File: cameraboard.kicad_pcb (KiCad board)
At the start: 4 copper layers, 46.1 x 45.6 mm, 93 parts, among them J1 USB_C_Receptacle_USB2.0, J2 02x05 M 1.27mm, J3 USD-1040310811, J4 MOLEX_5051102491, J5 TFM-110-12-X-D-A, J6 FLE-107-01-X-DV-A, Q1 SQ3495EV-T1, SW1 CAS-120TA, SW2 KMR2x, SW3 CAS-120TA, U1 STM32H743VITx, U2 WE-TVS-82400102, U3 XC6210B332MR-G, U4 AP7366-28W5-7, U5 TLV75515PDBVR, U6 LTC4412xS6, Y1 12MHz/7pF

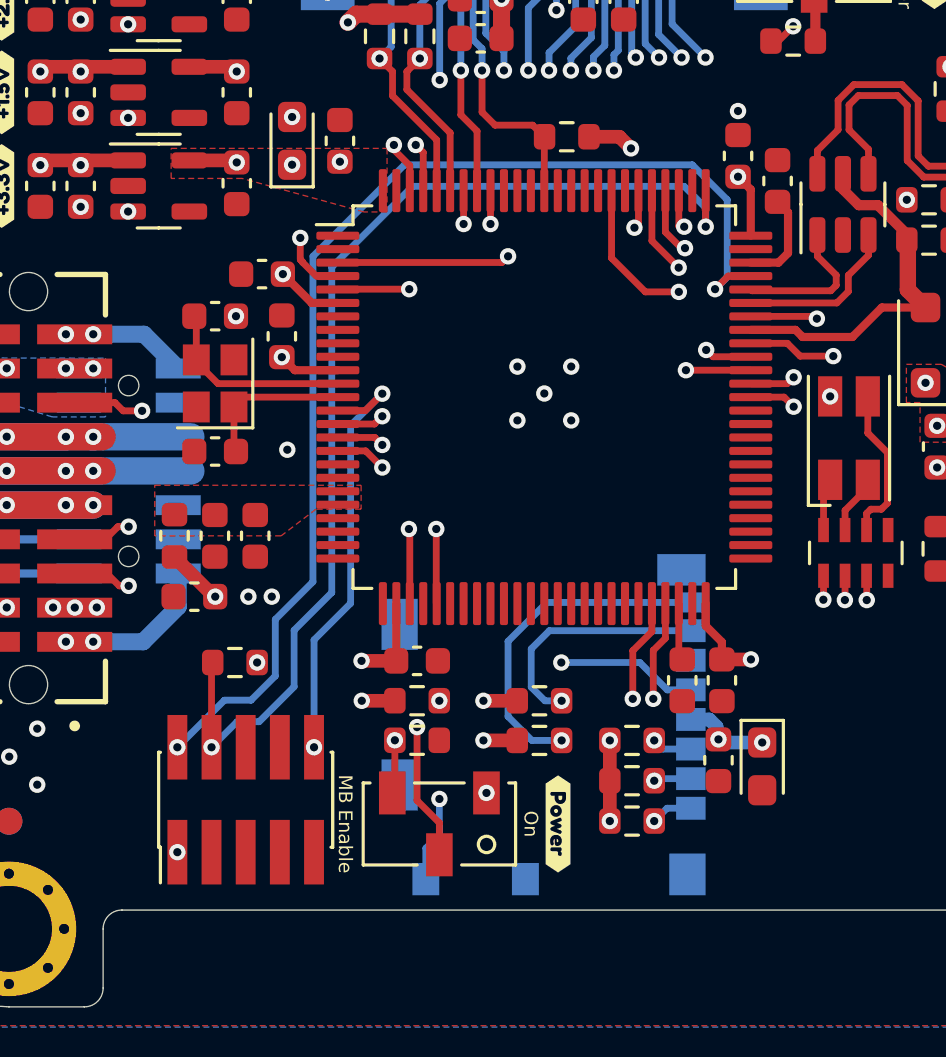
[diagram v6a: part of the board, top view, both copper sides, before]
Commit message: Moved SD card connector to allow removal with rails installed
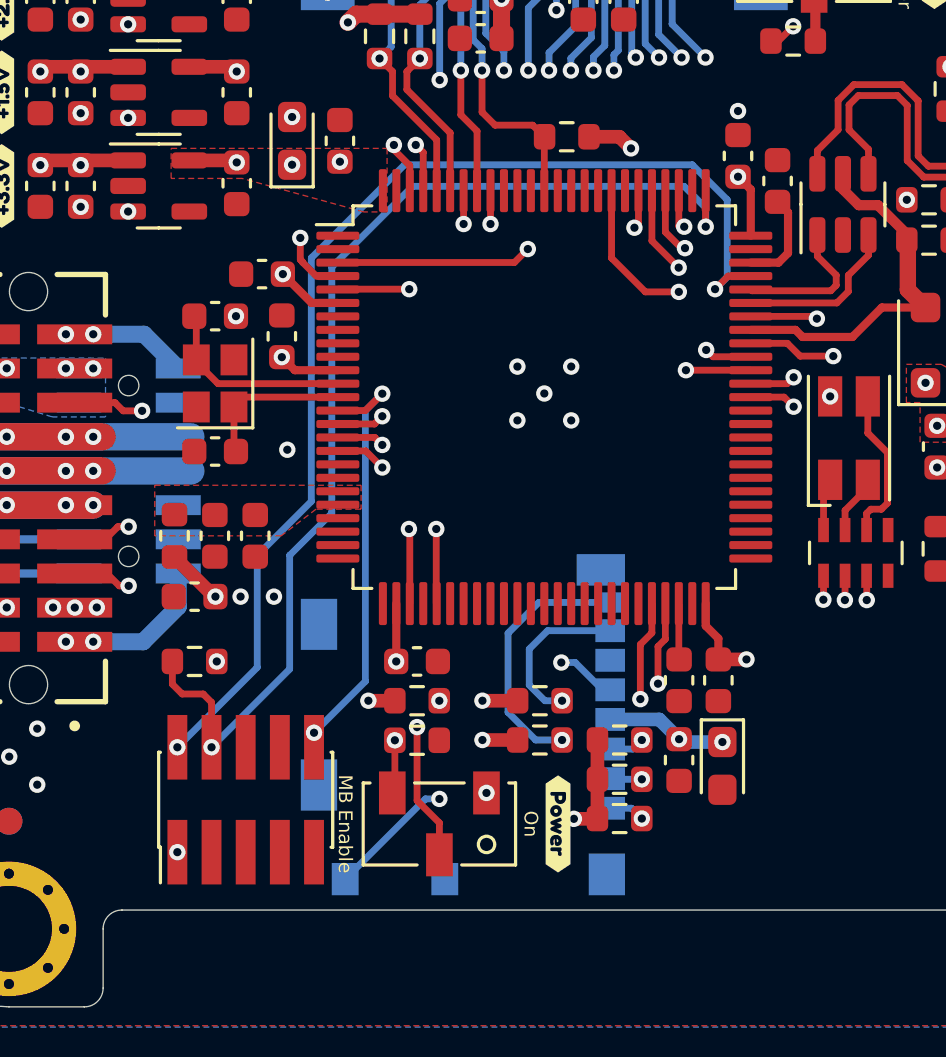
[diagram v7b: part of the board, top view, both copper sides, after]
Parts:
- moved J3 3.00 mm to (100.0, 78.5)
- moved Ref** 1.90 mm to (116.2, 78.2)
- moved R8 1.50 mm to (90.0, 76.2)
- moved C19 1.48 mm to (109.6, 80.0)
- moved C20 1.46 mm to (108.0, 79.8)
- moved R13 0.47 mm to (105.8, 82.0)
- moved R14 0.46 mm to (105.8, 80.5)
- moved R10 0.46 mm to (105.8, 79.1)
- moved C3 0.13 mm to (109.5, 76.9)
- moved C4 0.12 mm to (108.0, 76.9)
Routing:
- net /SDIO_CLK: track 25.5 -> 22.5 mm
- net /SDIO_D1: track 31.1 -> 28.2 mm
- net /SDIO_D0: track 25.6 -> 22.7 mm
- net /SD_CD: track 28.9 -> 30.4 mm
- net /SDIO_D2: track 32.9 -> 32.1 mm
- net /SDIO_D3: track 31.0 -> 30.4 mm
- net /SDIO_CMD: track 30.9 -> 30.2 mm
- net /SWCLK: track 40.9 -> 41.5 mm
- net /SWDIO: track 43.3 -> 42.7 mm
- net /NRST: track 48.5 -> 48.0 mm
- net +3.3V: track 32.3 -> 32.8 mm, vias 23 -> 22
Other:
- board text added: "18-JUN-23"
- board text removed: "12-JUN-23"

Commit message: PCB cleanup
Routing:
- net /UART3_RX: track 29.2 -> 28.0 mm
- net /UART3_TX: track 27.6 -> 26.5 mm
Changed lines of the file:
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@@
     (pts (xy 80.2 46.3) (xy 125.8 46.3))
     (height -6.93)
-    (gr_text "1795.2756 mils" (at 103 38.22) (layer "Dwgs.User")
+    (gr_text "45.6000 mm" (at 103 38.22) (layer "Dwgs.User")
       (effects (font (size 1 1) (thickness 0.15)))
     )
@@
     (pts (xy 83.1 43.4) (xy 83.100001 89))
     (height 7.157423)
-    (gr_text "1795.2756 mils" (at 77.092578 66.2 270.0000025) (layer "Dwgs.User")
+    (gr_text "45.6000 mm" (at 77.092578 66.2 270.0000025) (layer "Dwgs.User")
       (effects (font (size 1 1) (thickness 0.15)))
     )
@@
   )
   (segment (start 108 74.0094) (end 108 76.075) (width 0.254) (layer "F.Cu") (net 1))
-  (segment (start 108 76.075) (end 108.01 76.085) (width 0.254) (layer "F.Cu") (net 1))
   (segment (start 90.7273 73.7512) (end 89.2542 72.2781) (width 0.508) (layer "F.Cu") (net 2))
   (segment (start 100.7 77.62) (end 102 77.62) (width 0.508) (layer "F.Cu") (net 2))
@@
   (segment (start 97.4976 76.1388) (end 97.4976 74.0118) (width 0.3048) (layer "F.Cu") (net 2))
   (segment (start 96.008502 52.0982) (end 96.8756 52.0982) (width 0.635) (layer "F.Cu") (net 2))
-  (segment (start 104.965 82.01) (end 104.975 82) (width 0.508) (layer "F.Cu") (net 2))
   (segment (start 93.2434 64.8488) (end 93.729 65.3344) (width 0.3048) (layer "F.Cu") (net 2))
   (segment (start 94.3538 62.8344) (end 93.2818 61.7624) (width 0.3048) (layer "F.Cu") (net 2))
@@
   (segment (start 120.4722 67.1472) (end 120.7668 67.4418) (width 0.508) (layer "F.Cu") (net 28))
   (segment (start 113.075 51.292001) (end 113.075 53.1) (width 0.381) (layer "F.Cu") (net 29))
-  (segment (start 113.03 51.247001) (end 113.075 51.292001) (width 0.381) (layer "F.Cu") (net 29))
   (segment (start 101.4098 50.053) (end 101.4098 51.5262) (width 0.635) (layer "F.Cu") (net 40))
   (segment (start 101.4098 51.5262) (end 101.4098 52.9994) (width 0.635) (layer "F.Cu") (net 40))
@@
   (segment (start 84.0002 67.81) (end 86.2306 67.81) (width 1.016) (layer "B.Cu") (net 57))
   (segment (start 87.3453 66.8453) (end 87.041023 66.541023) (width 0.254) (layer "F.Cu") (net 59))
-  (segment (start 97.445 80.952001) (end 97.350001 81.047) (width 0.254) (layer "F.Cu") (net 59))
   (segment (start 88.05 66.8453) (end 87.3453 66.8453) (width 0.254) (layer "F.Cu") (net 59))
   (segment (start 87.041023 66.541023) (end 85.542972 66.541023) (width 0.254) (layer "F.Cu") (net 59))
@@
   (segment (start 110.675 63.8344) (end 112.3344 63.8344) (width 0.3048) (layer "F.Cu") (net 88))
   (segment (start 114.69 59.2) (end 114.1 58.61) (width 0.381) (layer "F.Cu") (net 88))
-  (segment (start 116.5125 60.5) (end 116.5125 60.3125) (width 0.381) (layer "F.Cu") (net 88))
   (segment (start 114.1 58.61) (end 114.1 58.0341) (width 0.381) (layer "F.Cu") (net 88))
   (segment (start 112.3344 63.8344) (end 112.598671 64.098671) (width 0.3048) (layer "F.Cu") (net 88))
@@
   (segment (start 105.9942 71.2724) (end 105.9942 62.4736) (width 0.254) (layer "In1.Cu") (net 96))
   (segment (start 102.0064 75.2602) (end 105.9942 71.2724) (width 0.254) (layer "In1.Cu") (net 96))
-  (segment (start 105.4736 80.54) (end 105.45 80.5164) (width 0.254) (layer "B.Cu") (net 96))
   (segment (start 106.625 80.54) (end 105.4736 80.54) (width 0.254) (layer "B.Cu") (net 96))
   (segment (start 107.994998 61.521729) (end 107 60.526731) (width 0.254) (layer "F.Cu") (net 97))
@@
   (segment (start 107.4928 64.1072) (end 107.4928 72.3387) (width 0.254) (layer "In1.Cu") (net 97))
   (segment (start 108.6 62.126731) (end 108.6 63) (width 0.254) (layer "In1.Cu") (net 97))
-  (segment (start 105.1664 77.2164) (end 105.45 77.2164) (width 0.254) (layer "B.Cu") (net 97))
   (segment (start 103.6315 76.2) (end 104.15 76.2) (width 0.254) (layer "B.Cu") (net 97))
   (segment (start 104.15 76.2) (end 105.1664 77.2164) (width 0.254) (layer "B.Cu") (net 97))
@@
   (segment (start 107.22572 76.986608) (end 107.22572 75.60428) (width 0.254) (layer "F.Cu") (net 130))
   (segment (start 87.55 73.35) (end 87.2 73.35) (width 0.254) (layer "F.Cu") (net 130))
-  (segment (start 86.741023 72.891023) (end 85.542972 72.891023) (width 0.254) (layer "F.Cu") (net 130))
   (segment (start 87.2 73.35) (end 86.741023 72.891023) (width 0.254) (layer "F.Cu") (net 130))
   (segment (start 107.22572 75.60428) (end 107.5 75.33) (width 0.254) (layer "F.Cu") (net 130))
@@
   (segment (start 89.8 71.9) (end 88.35 73.35) (width 0.254) (layer "In2.Cu") (net 130))
   (segment (start 107 75.1) (end 107 74.0094) (width 0.254) (layer "F.Cu") (net 131))
-  (segment (start 86.678977 71.621023) (end 85.542972 71.621023) (width 0.254) (layer "F.Cu") (net 131))
   (segment (start 87.55 71.15) (end 87.15 71.15) (width 0.254) (layer "F.Cu") (net 131))
   (segment (start 106.57 75.53) (end 107 75.1) (width 0.254) (layer "F.Cu") (net 131))
